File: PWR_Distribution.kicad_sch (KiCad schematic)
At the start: 42 parts, among them J1 CarPowerConnector, U22 AP64501SP-13, U7 LM76202QPWPRQ1

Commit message: think im done with schematic
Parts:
- removed C50: 100uF, symbol Device:C_Polarized
- removed C64, C66: nf, Capacitor_SMD:C_0402_1005Metric, symbol Device:C
- removed C65: 1.2nF, Capacitor_SMD:C_0402_1005Metric, symbol Device:C
- removed C67, C68, C69, C70: 10u, Capacitor_SMD:C_0805_2012Metric, symbol Device:C
- removed L4: 3.3uH, symbol Device:L
- removed R47: 10R, Resistor_SMD:R_0402_1005Metric, symbol Device:R
- removed R48: 20K 1%, Resistor_SMD:R_0402_1005Metric, symbol Device:R
- removed R49: 12K 1%, Resistor_SMD:R_0402_1005Metric, symbol Device:R
- removed R50: 2.2K 1%, Resistor_SMD:R_0402_1005Metric, symbol Device:R
- removed TP9: TestPoint, TestPoint:TestPoint_Pad_2.0x2.0mm, symbol Connector:TestPoint
- removed U22: AP64501SP-13, Package_SO:SOIC-8-1EP_3.9x4.9mm_P1.27mm_EP2.95x4.9mm_Mask2.71x3.4mm_ThermalVias, symbol CM4IO:AP64351
- added C50, C57: 10 u, symbol Device:C
- added C56: 10 n, symbol Device:C
- added C58: 100 n, symbol Device:C
- added C59: 2.7 n, symbol Device:C
- added C60: 33 p, symbol Device:C
- added C61: 22 u, symbol Device:C
- added IC4: AP64501QSP-13, SOIC127P600X163-9N, symbol AP64501QSP-13:AP64501QSP-13
- added L2: 4.7 u, symbol Device:L
- added R30: 15.8 k, symbol Device:R
- added R31: 52.3 k, symbol Device:R
- added R32: 10 k, symbol Device:R
- C62, C63: value 100n -> 22 u; footprint Capacitor_SMD:C_0402_1005Metric -> (none); Field4 Farnell -> (none); Field5 2611911 -> (none); Field6 RM EMK105 B7104KV-F -> (none); Field7 TAIYO YUDEN EUROPE GMBH -> (none); Field8 110091611 -> (none); Part Description 0.1uF 10% 16V Ceramic Capacitor X7R 0402 (1005 Metric) -> (none)
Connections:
- net +12V_PWR: now also C50.1, C57.1, IC4.2 (VIN), IC4.3 (EN)
- net +5V_PWR: now also C62.1, C63.1, C61.1, L2.2, R31.1
- net GND: now also C62.2, C50.2, C56.2, C57.2, C59.2, C60.2, C61.2, IC4.7 (GND), IC4.9 (EP), R32.2
- new net: C60.1, IC4.6 (COMP), R30.1
- new net: C59.1, R30.2
- new net: C56.1, IC4.4 (SS)
- new net: C58.1, IC4.1 (BST)
- new net: C58.2, IC4.8 (SW), L2.1
- new net: IC4.5 (FB), R31.2, R32.1
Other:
- note added: "+5v @ 5A PSU ( 7.5v-28v Input )"
- note removed: "+5v @ 3A PSU ( 7.5v-28v Input )"
- note removed: "5v @ 3A PSU"

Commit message: Rev A (#1)
* updated readme

* small changes for ravi

* silly mistake

* some stuff

* added parts to almost everything (except can xtal and fuses)

* fixed cap sizes, added remaining parts, fixed rtc battery

* review committee changes implmented

* fixed relevant erc errors

* layout 1.0 kinda done

* more compact

* can

* small notes

* added 3d models

* moved some stuff around

* Migrate to USB C and added some ESD protections on Vbus; might still have some issues

* fixed erc and removed old schematics

* updated power to 24V i think

* changed usb to be simpler (no inbuilt hub)

* layout draft

* moved everything to front & 0603'd stuff

* mostly routed, except highspeed

* added new power, but lowkey need to redo a bunch of shit

* ready to route high speed i believe

* changed a bunch of stuff, still have work

* fart

* poop

* my life is horrible

* moved things to their own sheets

* rrrrrrrr

* add new lib frfr

* Schem done? [plz full review], redoing layout

* I hate my life

* I'm unhappy with the state of the world

* rrr

* frank

* frank2

* Copy of I hate my life pt2.5 final final (3)

* wow everything could not be worse

* my life could not be worse right now

* frink

* frink2

* I plead that my suffering is nearing its end

* frink4

* lak

* chang

* imp

* fjfdsfdslk

* P/Ns

* silkscreens

* silkscreen n shit

* jlc shit

* mostly fixed alignment

* ravi

* stupid git

* fixed

* fixed again

---------

Co-authored-by: krazykrayon <krishparikh@utexas.edu>
Co-authored-by: Mikail Sadic <mikail.sadic@utexas.edu>
Co-authored-by: Frank Li <fxl77@my.utexas.edu>
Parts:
- removed C14, C55: 47uF, Capacitor_SMD:C_0805_2012Metric, symbol Device:C
- removed C36, C37, C38, C39, C40, C41: 10u 35v, Capacitor_SMD:C_0805_2012Metric, symbol Device:C
- removed C50, C57: 10 u, symbol Device:C
- removed C54: 100nF, Capacitor_SMD:C_0805_2012Metric, symbol Device:C
- removed C62, C63: 22 u, symbol Device:C
- removed D10: 3.3V, LED_SMD:LED_0805_2012Metric, symbol Device:LED
- removed D11: 12V, LED_SMD:LED_0805_2012Metric, symbol Device:LED
- removed D3: SD12_SOD323, Diode_SMD:D_SOD-323, symbol Diode:SD12_SOD323
- removed J1: CarPowerConnector, symbol utsvt-connectors:CarPowerConnector
- removed R40, R41: 10K, Resistor_SMD:R_0805_2012Metric, symbol Device:R
- removed R42, R7: 100k, Resistor_SMD:R_0805_2012Metric, symbol Device:R
- removed R43: 7.5K, Resistor_SMD:R_0805_2012Metric, symbol Device:R
- removed R46: 5k, Resistor_SMD:R_0805_2012Metric, symbol Device:R
- removed R8: 3k, Resistor_SMD:R_0805_2012Metric, symbol Device:R
- removed TP10: TestPoint, TestPoint:TestPoint_Pad_2.0x2.0mm, symbol Connector:TestPoint
- removed U7: LM76202QPWPRQ1, UTSVT_ICs:SOP65P640X120-17N, symbol utsvt-chips:LM76202QPWPRQ1
- added C18: 1uF, Capacitor_SMD:C_0805_2012Metric_Pad1.18x1.45mm_HandSolder, symbol Device:C
- added C19: 220nF, Capacitor_SMD:C_0805_2012Metric_Pad1.18x1.45mm_HandSolder, symbol Device:C
- added C27, C6: 10uF, Capacitor_SMD:C_0805_2012Metric_Pad1.18x1.45mm_HandSolder, symbol Device:C
- added C3, C5, C7: 100n, Capacitor_SMD:C_0603_1608Metric_Pad1.08x0.95mm_HandSolder, symbol Device:C
- added C8, C9: 22uF, Capacitor_SMD:C_0805_2012Metric_Pad1.18x1.45mm_HandSolder, symbol Device:C
- added D7: 5V PWR LED, LED_SMD:LED_0603_1608Metric_Pad1.05x0.95mm_HandSolder, symbol Device:LED
- added F1: 3568, Controls_Pi:FUSE_3568, symbol 3568:3568
- added IC3: LM74502HDDFR, UTSVT_Power_SP:SOT65P280X110-8N, symbol UTSVT_ICs:LM74502HDDFR
- added J1: CarLVPowerConnector, UTSVT_Connectors:Molex_Nano-Fit_105309-xx02_1x02_P2.50mm_Vertical, symbol utsvt_connectors:CarLVPowerConnector
- added J2: Display Breakout, UTSVT_Connectors:Molex_Nano-Fit_105309-xx02_1x02_P2.50mm_Vertical, symbol UTSVT_Connectors:CarLVPowerConnector
- added Q2, Q3: NVMFWS1D7N04XMT1G, Controls_Pi:NVMFWS3D0P04M8LT1G, symbol NVMFWS1D7N04XMT1G:NVMFWS1D7N04XMT1G
- added R13: 10k, Resistor_SMD:R_0603_1608Metric_Pad0.98x0.95mm_HandSolder, symbol Device:R_US
- added R14: 200k, Resistor_SMD:R_0603_1608Metric_Pad0.98x0.95mm_HandSolder, symbol Device:R_US
- added TP1, TP2, TP3: TestPoint, TestPoint:TestPoint_Pad_2.0x2.0mm, symbol Connector:TestPoint
- added Z1: SMAF4759A-TP, Diode_SMD:D_SMA, symbol UTSVT_Power:SMAF4749A-TP
- C56: value 10 n -> 10nF; footprint (none) -> Capacitor_SMD:C_0603_1608Metric_Pad1.08x0.95mm_HandSolder; JLC (none) -> C1589; P/N (none) -> MSASH168SB5103KTNA01
- C58: value 100 n -> 10uF; footprint (none) -> Capacitor_SMD:C_0805_2012Metric_Pad1.18x1.45mm_HandSolder; JLC (none) -> C440198; P/N (none) -> GRM21BR61H106KE43K
- C59: value 2.7 n -> 2.7nF; footprint (none) -> Capacitor_SMD:C_0603_1608Metric_Pad1.08x0.95mm_HandSolder; JLC (none) -> C107085; P/N (none) -> 08051C272J4Z2A
- C60: value 33 p -> 33pF; footprint (none) -> Capacitor_SMD:C_0603_1608Metric_Pad1.08x0.95mm_HandSolder; JLC (none) -> C1663; P/N (none) -> C0603X330M1HACTU
- C61: value 22 u -> 22uF; footprint (none) -> Capacitor_SMD:C_0805_2012Metric_Pad1.18x1.45mm_HandSolder; JLC (none) -> C338078; P/N (none) -> C2012X5R1V226M125AC
- D9: value 12V -> 24V PWR LED; footprint LED_SMD:LED_0805_2012Metric -> LED_SMD:LED_0603_1608Metric_Pad1.05x0.95mm_HandSolder; Color Green -> (none); If 2mA -> (none); Inventory Y -> (none); JLC (none) -> C2289; Mouser Part Number 604-APTD2012LCGCK -> (none); Mouser Price/Stock https://www.mouser.com/ProductDetail/Kingbright/APTD2012LCG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 -> (none); P/N APTD2012LCGCK -> 150060VS55040; Vf 1.9V -> (none)
- IC4: footprint SOIC127P600X163-9N -> Controls_Pi:SOIC127P600X163-9N; Height 1.63 -> (none); JLC (none) -> C2071517; Manufacturer_Name Diodes Incorporated -> (none); Manufacturer_Part_Number AP64501QSP-13 -> (none); Mouser Part Number 621-AP64501QSP-13 -> (none); Mouser Price/Stock https://www.mouser.co.uk/ProductDetail/Diodes-Incorporated/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 -> (none); P/N (none) -> AP64501QSP-13
- L2: value 4.7 u -> 4.7uH; footprint (none) -> Controls_Pi:INDPM110100X540N; JLC (none) -> C19947673; P/N (none) -> SRP1050WA-4R7M
- R30: value 15.8 k -> 15.8k; footprint (none) -> Resistor_SMD:R_0805_2012Metric_Pad1.20x1.40mm_HandSolder; JLC (none) -> C17468; P/N (none) -> AA0805FR-0715K8L
- R31: value 52.3 k -> 52.3k; footprint (none) -> Resistor_SMD:R_0805_2012Metric_Pad1.20x1.40mm_HandSolder; JLC (none) -> C22369875; P/N (none) -> RMCF0805FT52K3
- R32: value 10 k -> 10k; footprint (none) -> Resistor_SMD:R_0805_2012Metric; JLC (none) -> C17414; P/N (none) -> AC0805DR-0710KL
- R44: value 5k -> 1.5k; footprint Resistor_SMD:R_0805_2012Metric -> Resistor_SMD:R_0805_2012Metric_Pad1.20x1.40mm_HandSolder; Inventory Y -> (none); JLC (none) -> C417005; Mouser Part Number 71-CRCW0805-22.1K-E3 -> (none); Mouser Price/Stock https://www.mouser.com/ProductDetail/Vishay-Dale/CRCW080522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 -> (none); P/N CRCW080522K1FKEA -> ERJ-UP6F1501V
- R45: value 2.2k -> 200; footprint Resistor_SMD:R_0805_2012Metric -> Resistor_SMD:R_0603_1608Metric_Pad0.98x0.95mm_HandSolder; JLC (none) -> C8218; Mouser Part Number Inventory -> (none); P/N SDR10EZPF2200 -> SG73S1JTTD2000F
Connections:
- net GND: now also C58.2, C18.1, C27.2, C3.1, C6.2, C7.2, C8.2, C9.2, D7.1 (K), IC3.2 (GND), J1.2 (GND), J2.2 (GND), R13.2, TP3.1, Z1.2 (A)
- net at R45.2: now also D7.2 (A)
- net at IC4.1 (BST): now also C5.1; no longer C58.1
- net at IC4.8 (SW), L2.1: now also C5.2; no longer C58.2
- net +12V_PWR renamed +24V
- net +24V: now also C58.1, C27.1, C6.1, C7.1, F1.2, F1.4, Q3.5, Q3.6, Q3.7, Q3.8, Q3.9, TP1.1
- net +5V_PWR renamed +5V
- net +5V: now also C8.1, C9.1, TP2.1
- new net: IC3.8 (SRC), Q2.1, Q2.2, Q2.3, Q3.1, Q3.2, Q3.3
- new net: IC3.6 (GATE), Q2.4, Q3.4
- new net: C19.2, IC3.4 (VCAP)
- new net: IC3.7 (OV), R13.1, R14.2
- new net: F1.1, F1.3, J2.1 (+24V)
- new net LV+: C18.2, C19.1, C3.2, IC3.1 (EN/UVLO), IC3.5 (VS), J1.1 (+24V), Q2.5, Q2.6, Q2.7, Q2.8, Q2.9, R14.1, Z1.1 (K)
- no-connect marks 3 -> 0
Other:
- note added: "24V -> 5V BUCK"
- note added: "Display PWR"
- note added: "Est. max power draw (CM5) = 10W (pi) + 1.5W (HDMI) + 0.6W (CAN) = ~12.1W (rest of board draws negligible power)"
- note added: "Est. max power draw = 15W (pi) + 1.5W (HDMI) + 0.6W (CAN) = 21.6W (rest of board draws negligible power)"
- note added: "From VCU"
- note added: "LEDS"
- note added: "Power"
- note added: "R: ~1500 0.4W"
- note added: "R: ~200"
- note added: "RPP & OVP From VCU"
- note added: "Should be spec'd for CM5?"
- note added: "fwd cur: ~20ma fwd volt: ~2V"
- note added: "~26V OVP"
- note removed: "12V PWR"
- note removed: "5V PWR"
- note removed: "Current lim(A) = 12/Rilim(k) 1.7A = 12/7k ohms"
- note removed: "PWR FAULT"
- note removed: "RTN!=GND Conecting GND to RTN turns off RPP!"
- note removed: "Vin protection"
- moved on the sheet: C56, C59, C60, C61, D9, IC4, L2, R30, R31, R32, R44, R45

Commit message: poop
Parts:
- added C14, C2: 100uF, Capacitor_SMD:C_1206_3216Metric_Pad1.33x1.80mm_HandSolder, symbol Device:C
- added R10: 10k, Resistor_SMD:R_0603_1608Metric_Pad0.98x0.95mm_HandSolder, symbol Device:R_US
- L2: JLC C19947673 -> C5189748
- R31: value 52.3k -> 53.6k; JLC C22369875 -> C2930115; P/N RMCF0805FT52K3 -> FRC0603F5362TS
- R44: value 1.5k -> 3k; footprint Resistor_SMD:R_0805_2012Metric_Pad1.20x1.40mm_HandSolder -> Resistor_SMD:R_0603_1608Metric_Pad0.98x0.95mm_HandSolder; JLC C417005 -> C445829; P/N ERJ-UP6F1501V -> ERJPA3J302V
- R45: value 200 -> 400; JLC C8218 -> C5841024; P/N SG73S1JTTD2000F -> PAT0603E4000BST1
- Z1: now fitted
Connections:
- net +5V: now also C14.1, C2.1
- net GND: now also C14.2, C2.2
- net LV+: now also R10.1; no longer C18.2, C19.1, IC3.1 (EN/UVLO), IC3.5 (VS), Z1.1 (K)
- new net RPP_EN: C18.2, C19.1, IC3.1 (EN/UVLO), IC3.5 (VS), R10.2, Z1.1 (K)
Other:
- note added: "Fix"
- note added: "R: 3k 0.165W"
- note added: "Targeting 7.5mA"
- note added: "Targeting ~5.1V"
- note removed: "R: ~1500 0.4W"
- note removed: "R: ~200"

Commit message: poop
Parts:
- L2: P/N SRP1050WA-4R7M -> CYA0630-4.7UH
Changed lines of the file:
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@@
 			)
 		)
-		(property "Datasheet" "~"
+		(property "Datasheet" "https://jlcpcb.com/api/file/downloadByFileSystemAccessId/8589836786190225408"
 			(at 96.52 113.03 0)
 			(effects
@@
 			)
 		)
-		(property "P/N" " SRP1050WA-4R7M "
+		(property "P/N" "CYA0630-4.7UH"
 			(at 96.52 113.03 0)
 			(effects

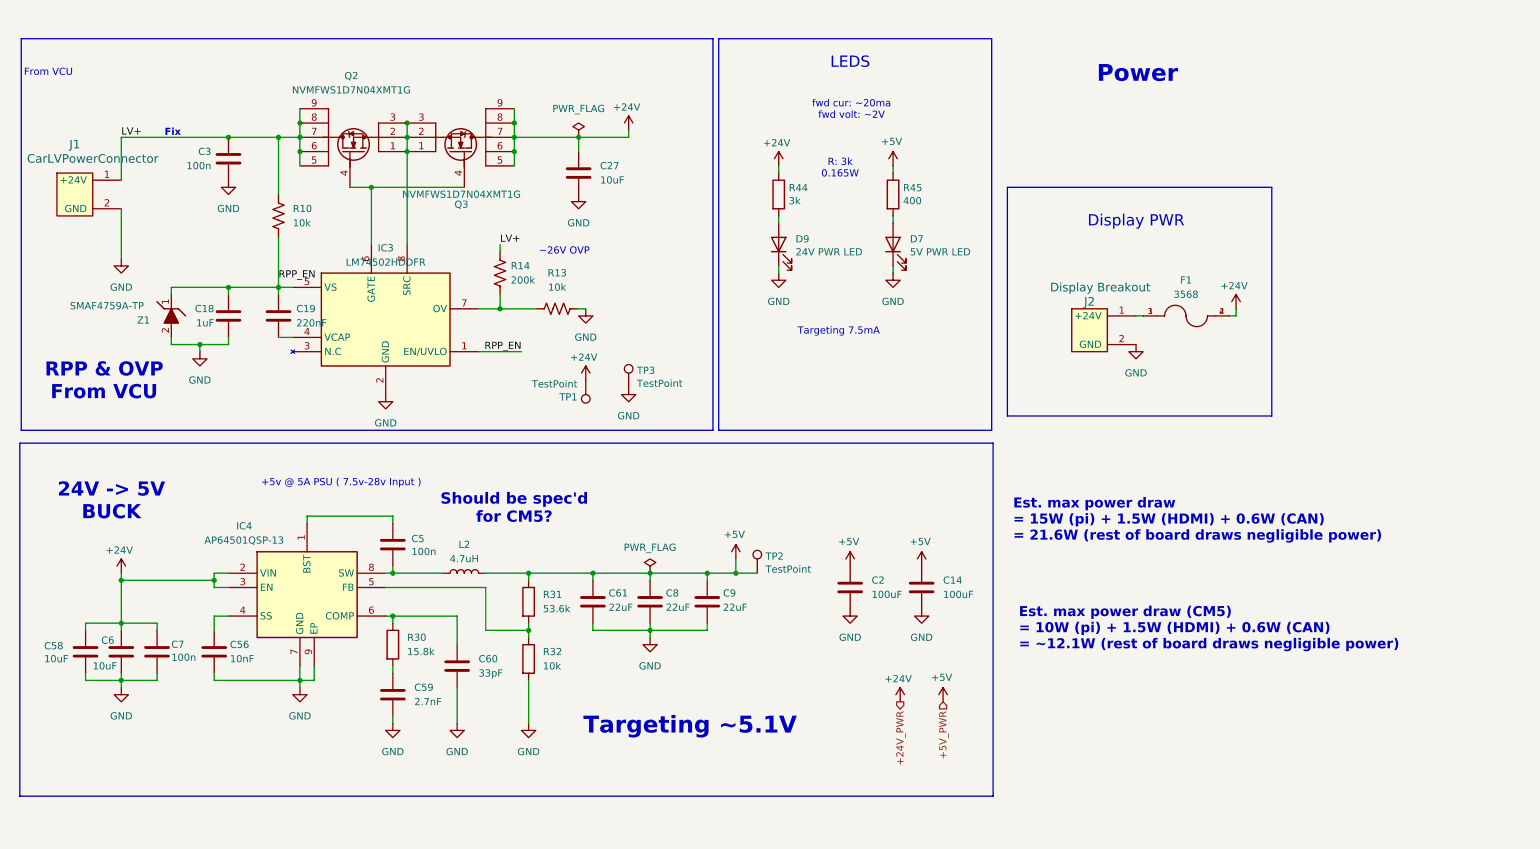
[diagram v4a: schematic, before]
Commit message: ideal diode circuit protection on usbc
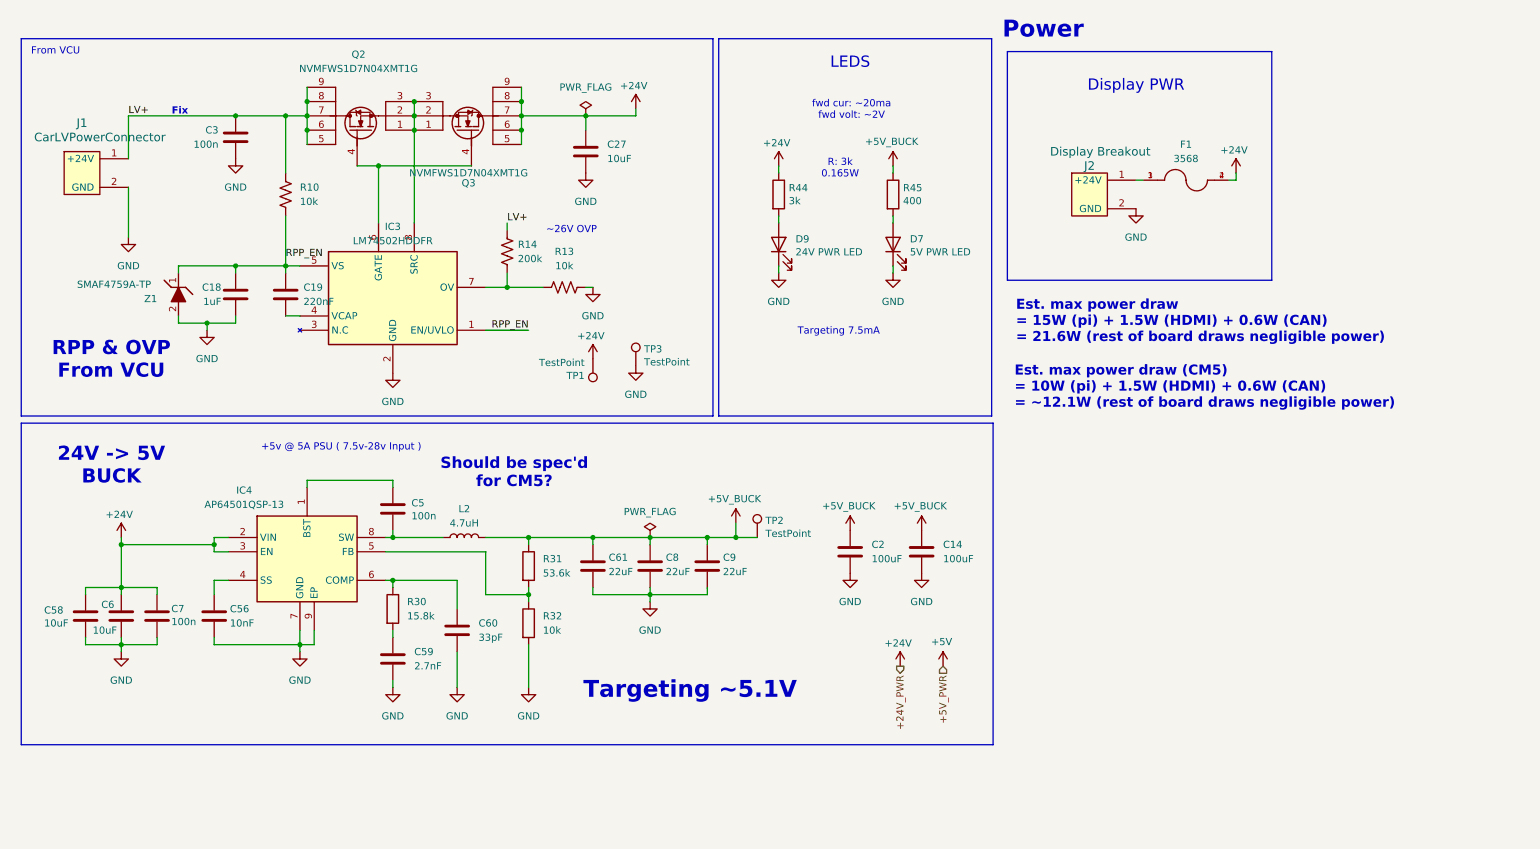
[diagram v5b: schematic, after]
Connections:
- net +5V: no longer C14.1, C2.1, C61.1, C8.1, C9.1, L2.2, R31.1, R45.1, TP2.1
- new net +5V_BUCK: C14.1, C2.1, C61.1, C8.1, C9.1, L2.2, R31.1, R45.1, TP2.1
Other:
- moved on the sheet: C14, C18, C19, C2, C27, C3, C5, C56, C58, C59, C6, C60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
